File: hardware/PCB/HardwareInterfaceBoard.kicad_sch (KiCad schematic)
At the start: 74 parts, among them J1 Relay Board Connector, J11 Feed Sensor R2, J14 Left LEDs, J15 Right LEDs, J16 Reset, J17 Shutdown, J2 Pi 5V, J20 EXT, J24 Raspberry Pi GPIO header, J25 RTC Header, J26 I2C0, J27 I2C1, J28 I2C2, J29 I2C3, J3 Display 5V, J30 I2C4, J31 I2C5, J32 I2C6, J33 I2C7, J4 DC 5V, J6 Feed Sensor L1, J7 Power bus, J8 Feed Sensor R1, J9 Feed Sensor L2, Q1 PN2222A, Q2 PN2222A, Q3 PN2222A, Q4 PN2222A, Q5 PN2222A, Q6 PN2222A, Q7 PN2222A, Q8 PN2222A, SW1 Pico Reset, U1 Raspberry Pico, U2 74HC595, U3 TCA9548A, U4 LM1117, U5 DS3231MZ, U6 74HC165

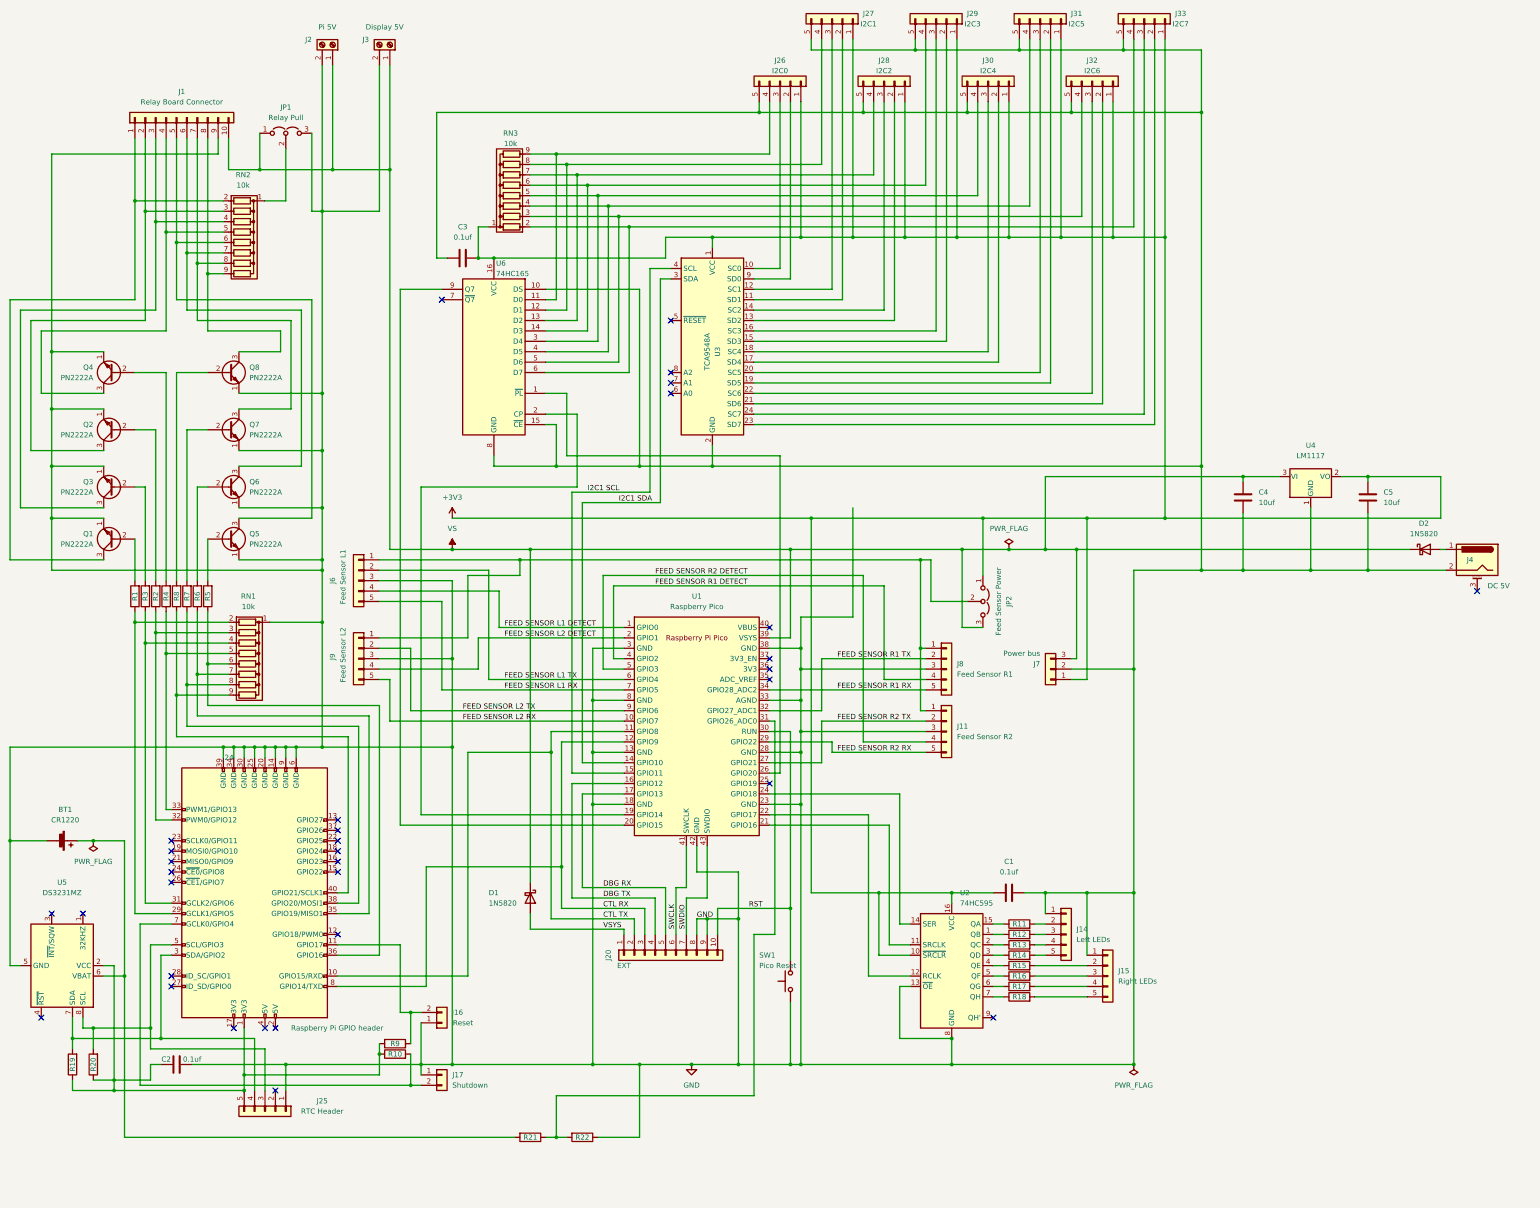
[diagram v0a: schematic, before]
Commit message: Trying to free up Pico pins by using another shift register
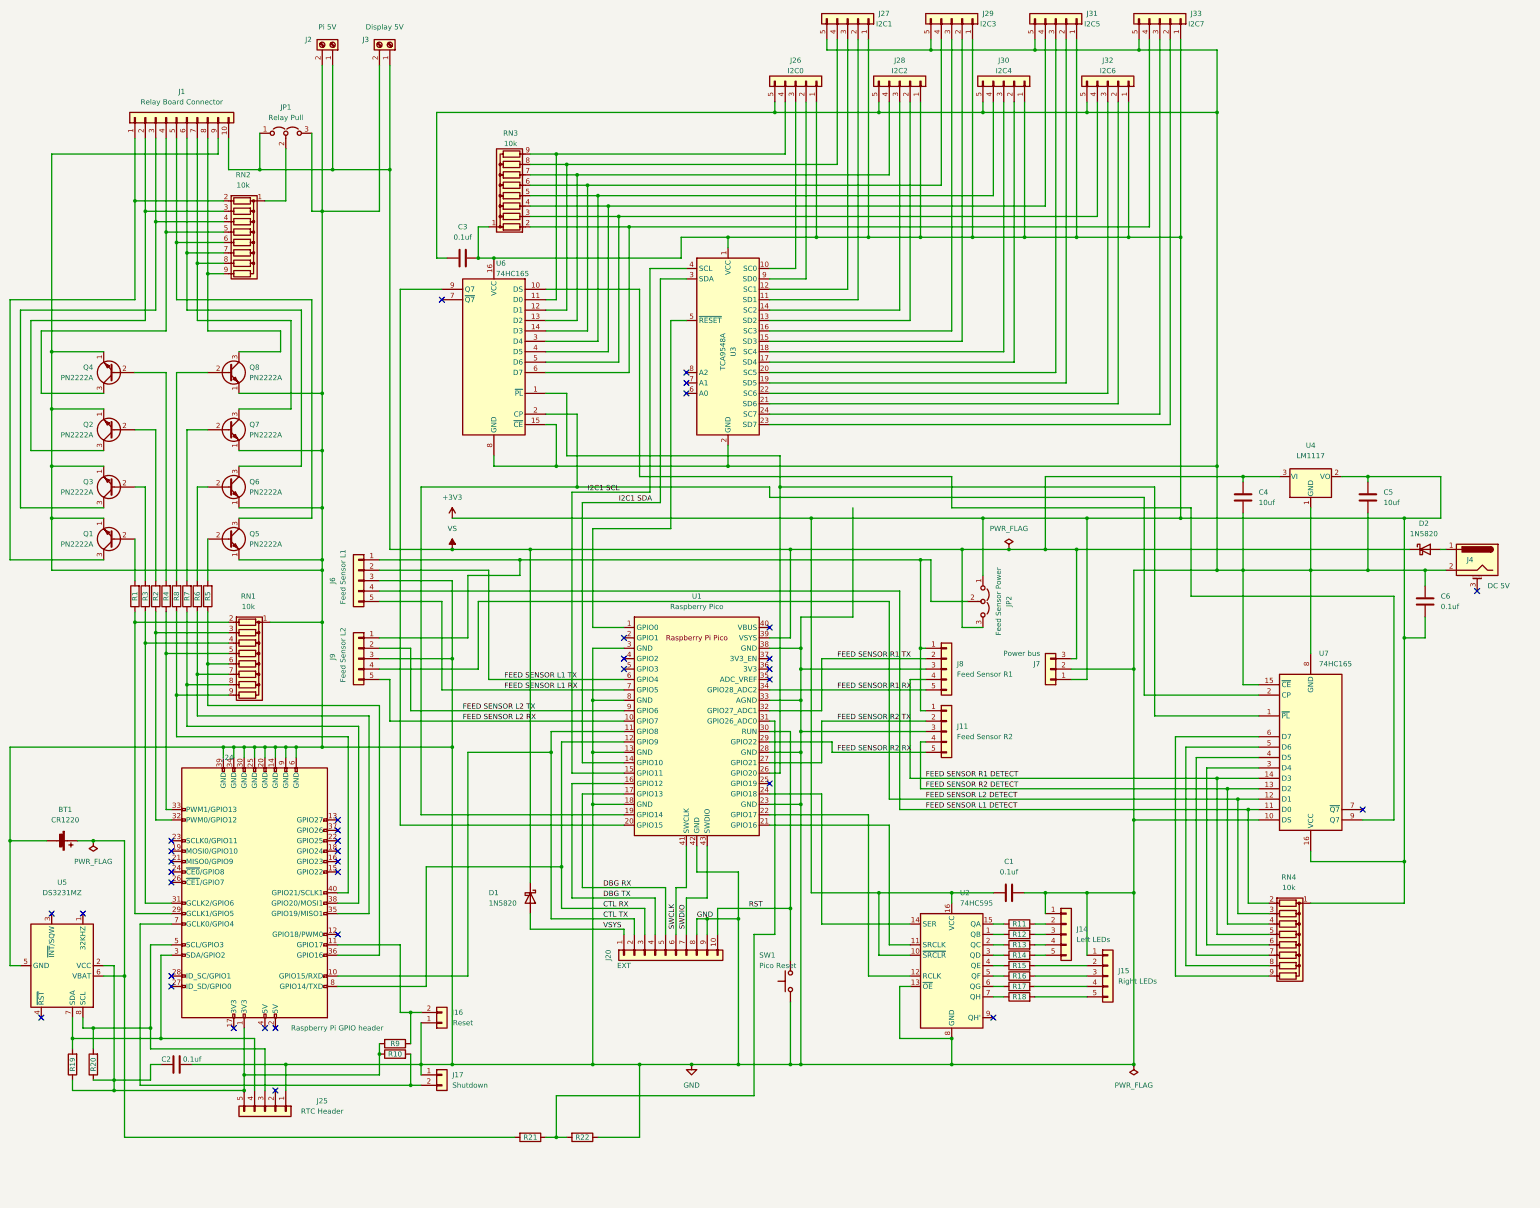
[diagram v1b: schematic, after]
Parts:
- added C6: 0.1uf, Capacitor_THT:C_Disc_D6.0mm_W2.5mm_P5.00mm, symbol Device:C
- added RN4: 10k, Resistor_THT:R_Array_SIP9, symbol Device:R_Network08
- added U7: 74HC165, Package_DIP:DIP-16_W7.62mm, symbol 74xx:74HC165
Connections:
- net +3V3: now also C6.2, RN4.1 (common), U7.16 (VCC)
- net FEED SENSOR L1 DETECT: now also RN4.2 (R1), U7.11 (D0); no longer U1.1 (GPIO0)
- net FEED SENSOR L2 DETECT: now also RN4.3 (R2), U7.12 (D1); no longer U1.2 (GPIO1)
- net FEED SENSOR R1 DETECT: now also RN4.5 (R4), U7.14 (D3); no longer U1.4 (GPIO2)
- net FEED SENSOR R2 DETECT: now also RN4.4 (R3), U7.13 (D2); no longer U1.5 (GPIO3)
- net GND: now also C6.1, U7.10 (DS), U7.15 (~{CE}), U7.8 (GND); no longer U6.10 (DS)
- net at U1.26 (GPIO20), U6.1 (~{PL}): now also U7.1 (~{PL})
- net at U1.19 (GPIO14), U6.2 (CP): now also U7.2 (CP)
- net at U3.5 (~{RESET}): now also U1.1 (GPIO0)
- new net: U6.10 (DS), U7.9 (Q7)
- new net: RN4.6 (R5), U7.3 (D4)
- new net: RN4.7 (R6), U7.4 (D5)
- new net: RN4.8 (R7), U7.5 (D6)
- new net: RN4.9 (R8), U7.6 (D7)
- no-connect marks 33 -> 36
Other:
- moved on the sheet: J26, J27, J28, J29, J30, J31, J32, J33, U3

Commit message: Board arrangement/tidying
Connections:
- net FEED SENSOR L1 DETECT: now also RN4.5 (R4); no longer RN4.2 (R1)
- net FEED SENSOR L2 DETECT: now also RN4.4 (R3); no longer RN4.3 (R2)
- net FEED SENSOR R1 DETECT: now also RN4.2 (R1); no longer RN4.5 (R4)
- net FEED SENSOR R2 DETECT: now also RN4.3 (R2); no longer RN4.4 (R3)
- net at U3.5 (~{RESET}): now also U1.2 (GPIO1); no longer U1.1 (GPIO0)
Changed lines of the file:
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@@
   (junction (at 240.03 191.77) (diameter 0) (color 0 0 0 0)
   )
+  (junction (at 415.29 247.65) (diameter 0) (color 0 0 0 0)
+  )
   (junction (at 246.38 171.45) (diameter 0) (color 0 0 0 0)
   )
@@
   (junction (at 156.21 224.79) (diameter 0) (color 0 0 0 0)
   )
-  (junction (at 412.75 252.73) (diameter 0) (color 0 0 0 0)
-  )
   (junction (at 387.35 257.81) (diameter 0) (color 0 0 0 0)
   )
@@
   (junction (at 138.43 321.31) (diameter 0) (color 0 0 0 0)
   )
+  (junction (at 407.67 255.27) (diameter 0) (color 0 0 0 0)
+  )
   (junction (at 255.27 228.6) (diameter 0) (color 0 0 0 0)
   )
@@
   (junction (at 407.67 171.45) (diameter 0) (color 0 0 0 0)
   )
-  (junction (at 410.21 250.19) (diameter 0) (color 0 0 0 0)
-  )
   (junction (at 148.59 111.76) (diameter 0) (color 0 0 0 0)
   )
@@
   (junction (at 309.88 115.57) (diameter 0) (color 0 0 0 0)
   )
+  (junction (at 410.21 252.73) (diameter 0) (color 0 0 0 0)
+  )
   (junction (at 148.59 212.09) (diameter 0) (color 0 0 0 0)
   )
@@
   (junction (at 133.35 262.89) (diameter 0) (color 0 0 0 0)
   )
-  (junction (at 407.67 247.65) (diameter 0) (color 0 0 0 0)
-  )
   (junction (at 444.5 196.85) (diameter 0) (color 0 0 0 0)
   )
@@
   (junction (at 251.46 100.33) (diameter 0) (color 0 0 0 0)
   )
-  (junction (at 415.29 255.27) (diameter 0) (color 0 0 0 0)
-  )
   (junction (at 303.53 317.5) (diameter 0) (color 0 0 0 0)
   )
@@
   )
   (junction (at 189.23 196.85) (diameter 0) (color 0 0 0 0)
+  )
+  (junction (at 412.75 250.19) (diameter 0) (color 0 0 0 0)
   )
   (junction (at 189.23 153.67) (diameter 0) (color 0 0 0 0)
@@
   (no_connect (at 262.89 220.98))
   (no_connect (at 262.89 218.44))
-  (no_connect (at 262.89 213.36))
+  (no_connect (at 262.89 210.82))
   (no_connect (at 177.8 308.61))
   (no_connect (at 471.17 201.93))
@@
     (stroke (width 0) (type default) (color 0 0 0 0))
   )
-  (wire (pts (xy 412.75 252.73) (xy 417.83 252.73))
+  (wire (pts (xy 327.66 252.73) (xy 410.21 252.73))
     (stroke (width 0) (type default) (color 0 0 0 0))
   )
@@
     (stroke (width 0) (type default) (color 0 0 0 0))
   )
+  (wire (pts (xy 412.75 250.19) (xy 412.75 280.67))
+    (stroke (width 0) (type default) (color 0 0 0 0))
+  )
   (wire (pts (xy 327.66 100.33) (xy 327.66 82.55))
     (stroke (width 0) (type default) (color 0 0 0 0))
@@
     (stroke (width 0) (type default) (color 0 0 0 0))
   )
+  (wire (pts (xy 407.67 255.27) (xy 417.83 255.27))
+    (stroke (width 0) (type default) (color 0 0 0 0))
+  )
   (wire (pts (xy 363.22 69.85) (xy 337.82 69.85))
     (stroke (width 0) (type default) (color 0 0 0 0))
@@
     (stroke (width 0) (type default) (color 0 0 0 0))
   )
-  (wire (pts (xy 415.29 255.27) (xy 415.29 278.13))
-    (stroke (width 0) (type default) (color 0 0 0 0))
-  )
   (wire (pts (xy 278.13 285.75) (xy 278.13 276.86))
     (stroke (width 0) (type default) (color 0 0 0 0))
@@
     (stroke (width 0) (type default) (color 0 0 0 0))
   )
+  (wire (pts (xy 412.75 250.19) (xy 417.83 250.19))
+    (stroke (width 0) (type default) (color 0 0 0 0))
+  )
   (wire (pts (xy 347.98 67.31) (xy 347.98 115.57))
     (stroke (width 0) (type default) (color 0 0 0 0))
@@
     (stroke (width 0) (type default) (color 0 0 0 0))
   )
-  (wire (pts (xy 417.83 255.27) (xy 415.29 255.27))
-    (stroke (width 0) (type default) (color 0 0 0 0))
-  )
   (wire (pts (xy 306.07 215.9) (xy 306.07 220.98))
     (stroke (width 0) (type default) (color 0 0 0 0))
@@
     (stroke (width 0) (type default) (color 0 0 0 0))
   )
+  (wire (pts (xy 407.67 255.27) (xy 407.67 285.75))
+    (stroke (width 0) (type default) (color 0 0 0 0))
+  )
   (wire (pts (xy 365.76 275.59) (xy 375.92 275.59))
     (stroke (width 0) (type default) (color 0 0 0 0))
@@
     (stroke (width 0) (type default) (color 0 0 0 0))
   )
+  (wire (pts (xy 410.21 252.73) (xy 410.21 283.21))
+    (stroke (width 0) (type default) (color 0 0 0 0))
+  )
   (wire (pts (xy 144.78 283.21) (xy 152.4 283.21))
     (stroke (width 0) (type default) (color 0 0 0 0))
@@
     (stroke (width 0) (type default) (color 0 0 0 0))
   )
-  (wire (pts (xy 327.66 252.73) (xy 412.75 252.73))
-    (stroke (width 0) (type default) (color 0 0 0 0))
-  )
   (wire (pts (xy 375.92 184.15) (xy 375.92 223.52))
     (stroke (width 0) (type default) (color 0 0 0 0))
@@
     (stroke (width 0) (type default) (color 0 0 0 0))
   )
+  (wire (pts (xy 262.89 213.36) (xy 255.27 213.36))
+    (stroke (width 0) (type default) (color 0 0 0 0))
+  )
   (wire (pts (xy 177.8 240.03) (xy 180.34 240.03))
     (stroke (width 0) (type default) (color 0 0 0 0))
@@
     (stroke (width 0) (type default) (color 0 0 0 0))
   )
+  (wire (pts (xy 255.27 186.69) (xy 255.27 213.36))
+    (stroke (width 0) (type default) (color 0 0 0 0))
+  )
   (wire (pts (xy 255.27 317.5) (xy 266.7 317.5))
     (stroke (width 0) (type default) (color 0 0 0 0))
@@
     (stroke (width 0) (type default) (color 0 0 0 0))
   )
-  (wire (pts (xy 412.75 280.67) (xy 412.75 252.73))
-    (stroke (width 0) (type default) (color 0 0 0 0))
-  )
   (wire (pts (xy 283.21 281.94) (xy 290.83 281.94))
     (stroke (width 0) (type default) (color 0 0 0 0))
@@
     (stroke (width 0) (type default) (color 0 0 0 0))
   )
+  (wire (pts (xy 410.21 252.73) (xy 417.83 252.73))
+    (stroke (width 0) (type default) (color 0 0 0 0))
+  )
   (wire (pts (xy 290.83 317.5) (xy 303.53 317.5))
     (stroke (width 0) (type default) (color 0 0 0 0))
@@
     (stroke (width 0) (type default) (color 0 0 0 0))
   )
-  (wire (pts (xy 330.2 255.27) (xy 415.29 255.27))
+  (wire (pts (xy 330.2 255.27) (xy 407.67 255.27))
     (stroke (width 0) (type default) (color 0 0 0 0))
   )
@@
     (stroke (width 0) (type default) (color 0 0 0 0))
   )
+  (wire (pts (xy 415.29 247.65) (xy 417.83 247.65))
+    (stroke (width 0) (type default) (color 0 0 0 0))
+  )
   (wire (pts (xy 180.34 106.68) (xy 180.34 93.98))
     (stroke (width 0) (type default) (color 0 0 0 0))
   )
-  (wire (pts (xy 407.67 285.75) (xy 407.67 247.65))
-    (stroke (width 0) (type default) (color 0 0 0 0))
-  )
   (wire (pts (xy 401.32 181.61) (xy 401.32 203.2))
     (stroke (width 0) (type default) (color 0 0 0 0))
   )
-  (wire (pts (xy 332.74 247.65) (xy 407.67 247.65))
+  (wire (pts (xy 332.74 247.65) (xy 415.29 247.65))
     (stroke (width 0) (type default) (color 0 0 0 0))
   )
@@
     (stroke (width 0) (type default) (color 0 0 0 0))
   )
-  (wire (pts (xy 262.89 210.82) (xy 255.27 210.82))
-    (stroke (width 0) (type default) (color 0 0 0 0))
-  )
   (wire (pts (xy 208.28 128.27) (xy 218.44 128.27))
     (stroke (width 0) (type default) (color 0 0 0 0))
@@
     (stroke (width 0) (type default) (color 0 0 0 0))
   )
+  (wire (pts (xy 415.29 247.65) (xy 415.29 278.13))
+    (stroke (width 0) (type default) (color 0 0 0 0))
+  )
   (wire (pts (xy 161.29 189.23) (xy 161.29 199.39))
     (stroke (width 0) (type default) (color 0 0 0 0))
@@
     (stroke (width 0) (type default) (color 0 0 0 0))
   )
-  (wire (pts (xy 417.83 250.19) (xy 410.21 250.19))
-    (stroke (width 0) (type default) (color 0 0 0 0))
-  )
   (wire (pts (xy 444.5 182.88) (xy 444.5 196.85))
     (stroke (width 0) (type default) (color 0 0 0 0))
   )
-  (wire (pts (xy 255.27 210.82) (xy 255.27 186.69))
-    (stroke (width 0) (type default) (color 0 0 0 0))
-  )
   (wire (pts (xy 189.23 181.61) (xy 189.23 194.31))
     (stroke (width 0) (type default) (color 0 0 0 0))
@@
     (stroke (width 0) (type default) (color 0 0 0 0))
   )
-  (wire (pts (xy 410.21 250.19) (xy 410.21 283.21))
-    (stroke (width 0) (type default) (color 0 0 0 0))
-  )
   (wire (pts (xy 220.98 317.5) (xy 255.27 317.5))
     (stroke (width 0) (type default) (color 0 0 0 0))
@@
     (stroke (width 0) (type default) (color 0 0 0 0))
   )
-  (wire (pts (xy 410.21 250.19) (xy 335.28 250.19))
+  (wire (pts (xy 335.28 250.19) (xy 412.75 250.19))
     (stroke (width 0) (type default) (color 0 0 0 0))
   )
@@
     (stroke (width 0) (type default) (color 0 0 0 0))
   )
-  (wire (pts (xy 407.67 247.65) (xy 417.83 247.65))
-    (stroke (width 0) (type default) (color 0 0 0 0))
-  )
